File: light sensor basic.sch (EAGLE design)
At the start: 1 part

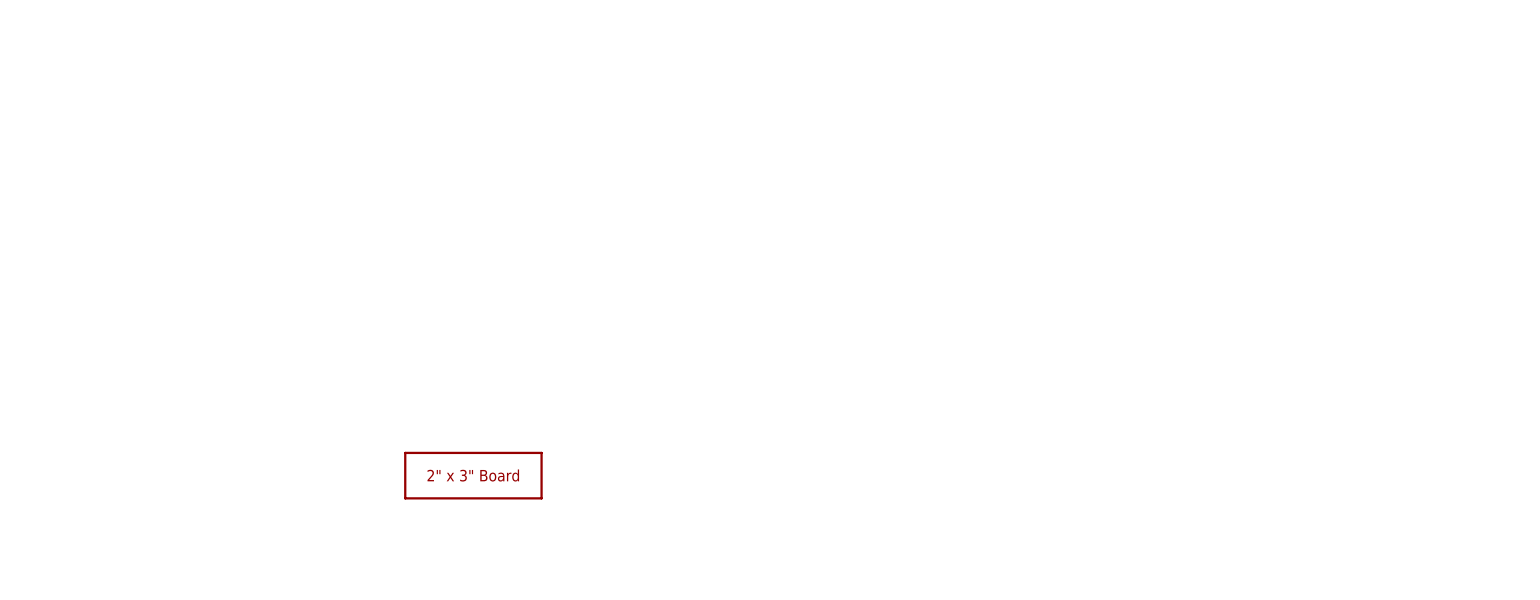
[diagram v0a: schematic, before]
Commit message: Update light sensor basic.sch
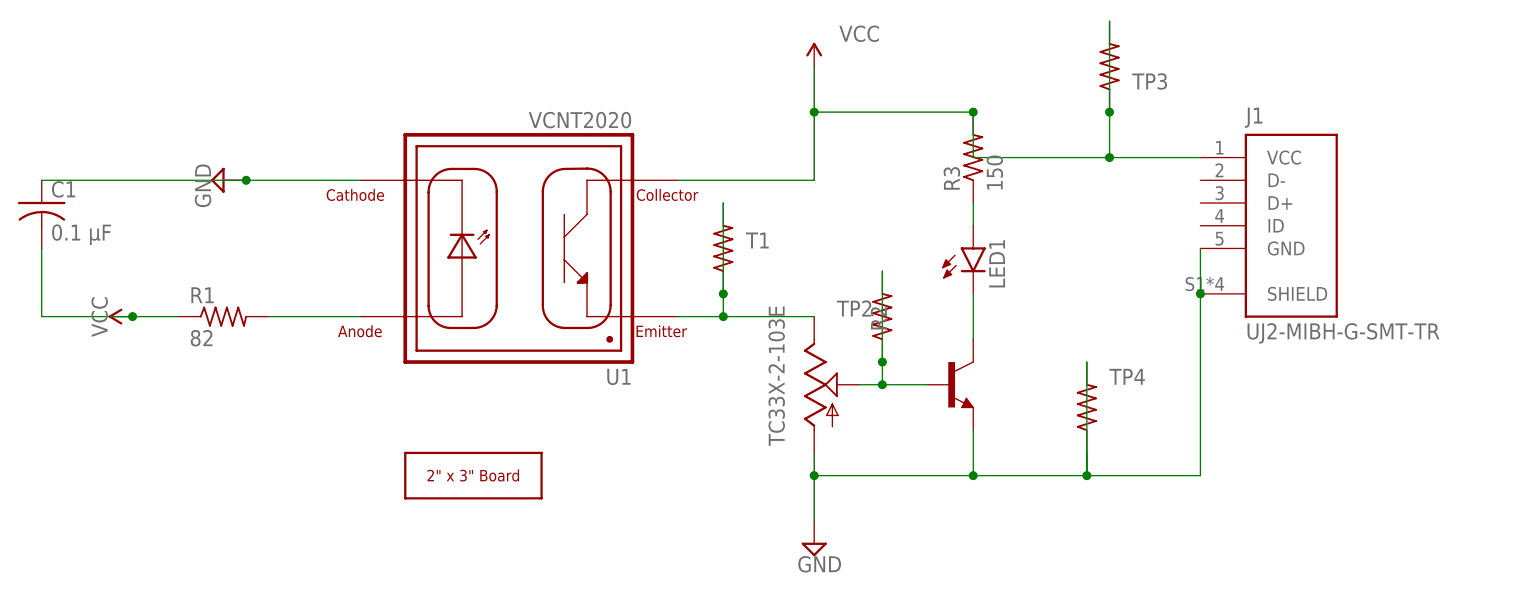
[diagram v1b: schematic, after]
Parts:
- added C1: 0.1 µF, rcl:C-USC0805
- added J1: UJ2-MIBH-G-SMT-TR, UJ2-MIBH-G-SMT-TR:UJ2-MIBH-G-SMT-TR
- added LED1: (no value), led:LEDSML0805
- added R1: 82, rcl:R-US_R0805
- added R2: TC33X-2-103E, Resistor_Capacitor:TC33X-2-103E
- added R3: 150, rcl:R-US_R0805
- added R4, R5: (no value), rcl:R-US_M1206
- added R6, R7: (no value), rcl:R-US_R0805
- added T1: (no value), transistor:-NPN-SOT23-EBC
- added U1: VCNT2020, VCNT2020:VCNT2020
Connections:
- new net GND: C1.1, U1.CATHODE
- new net N$1: R1.2, U1.ANODE
- new net N$3: LED1.C, T1.C
- new net N$4: R2.2, R7.1, R7.2, T1.B
- new net N$5: LED1.A, R3.1
- new net TP2: R2.1, R6.1, R6.2, U1.EMITTER
- new net TP3: J1.VCC, R3.2, R5.1, R5.2, U1.COLLECTOR
- new net TP4: J1.GND, J1.SHIELD, R2.3, R4.1, R4.2, T1.E
- new net VCC: C1.2, R1.1
